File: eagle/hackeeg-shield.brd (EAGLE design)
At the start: 101.6 x 53.3 mm, 145 parts, among them IC1 ADS1299IPAG, IC10 TXB0108PWR, IC11 TXB0108PWR, IC2 TPS72325DBVT, IC3 TPS73225DBVT, IC5 24AA256UID, IC6 TPS60403DBVT, IC7 OPA376DBV, IC8 OPA376DBV, IC9 TXS0102DCUR

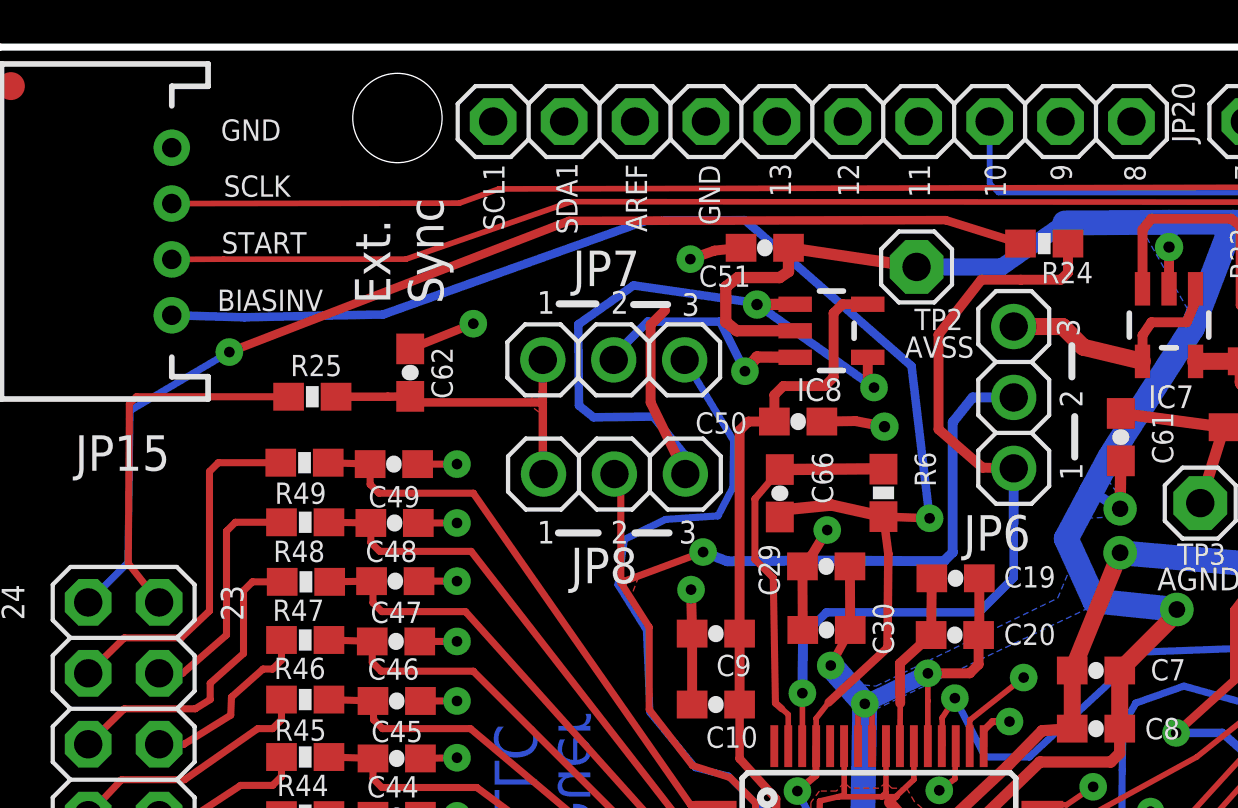
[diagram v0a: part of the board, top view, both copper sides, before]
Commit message: add option to put biasout on ext sync connector
- probably won't use this option, saving it just in case
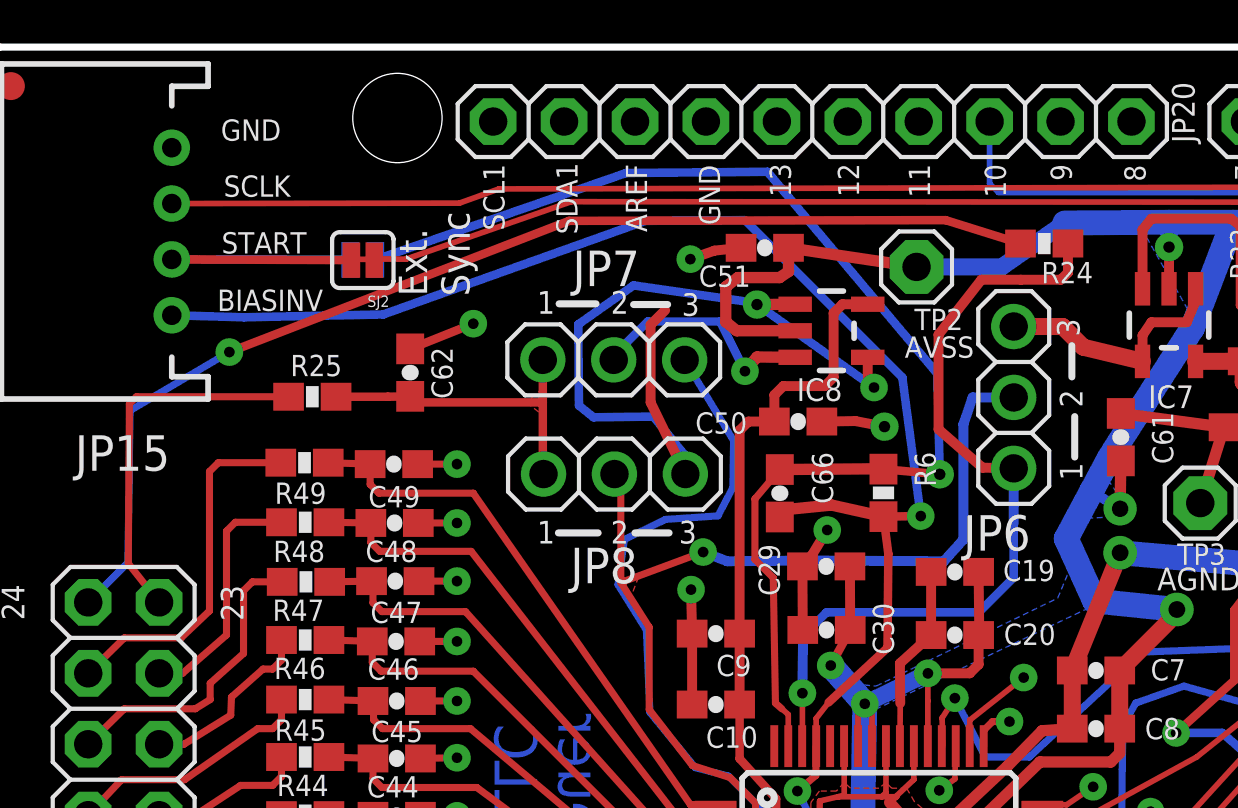
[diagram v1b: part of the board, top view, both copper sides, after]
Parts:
- added SJ1: SOLDERJUMPERNO, SparkFun-Passives:SJ_2S-NO
- added SJ2: SOLDERJUMPERNC, SparkFun-Passives:SJ_2S
- moved C19 0.23 mm to (35.3, 34.7)
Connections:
- new net SYNC_CONN_2: JP15.2, SJ1.2, SJ2.2
- net ADS_START: now also SJ2.1; no longer JP15.2
- net BIASOUT: now also SJ1.1
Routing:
- net BIASOUT: track 14.4 -> 44.1 mm, vias 0 -> 1
- net SYNC_CONN_2: track 0.00 -> 12.8 mm
- net ADS_START: track 118.6 -> 111.4 mm
- net N$22: track 0.00 -> 0.90 mm
- net BIASINV: track 89.9 -> 89.2 mm
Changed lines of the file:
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@@
 <layer number="20" name="Dimension" color="15" fill="1" visible="yes" active="yes"/>
 <layer number="21" name="tPlace" color="7" fill="1" visible="yes" active="yes"/>
-<layer number="22" name="bPlace" color="7" fill="1" visible="no" active="yes"/>
+<layer number="22" name="bPlace" color="7" fill="1" visible="yes" active="yes"/>
 <layer number="23" name="tOrigins" color="15" fill="1" visible="yes" active="yes"/>
-<layer number="24" name="bOrigins" color="15" fill="1" visible="no" active="yes"/>
+<layer number="24" name="bOrigins" color="15" fill="1" visible="yes" active="yes"/>
 <layer number="25" name="tNames" color="7" fill="1" visible="yes" active="yes"/>
 <layer number="26" name="bNames" color="7" fill="1" visible="no" active="yes"/>
@@
 <text x="62.0522" y="23.9776" size="0.8128" layer="21" font="vector" ratio="12" rot="R90">RST</text>
 <text x="9.144" y="48.1076" size="0.762" layer="21" font="vector" ratio="12">SCLK</text>
-<text x="17.018" y="44.2722" size="1.27" layer="21" font="vector" ratio="12" rot="R90">Ext.
+<text x="17.955515625" y="44.54880625" size="1.016" layer="21" font="vector" ratio="12" rot="R90">Ext.
 Sync</text>
 <text x="9.0424" y="50.1142" size="0.762" layer="21" font="vector" ratio="12">GND</text>
@@
 <attribute name="VALUE" x="36.068" y="14.1478" size="0.4064" layer="27" font="vector" rot="R270"/>
 </element>
-<element name="C19" library="SparkFun-Passives" package="0603-CAP" value="1uF" x="35.3568" y="34.4424" smashed="yes">
-<attribute name="NAME" x="37.084" y="34.1122" size="0.762" layer="25" font="vector" ratio="12"/>
-<attribute name="VALUE" x="34.3408" y="33.2994" size="0.4064" layer="27" font="vector"/>
+<element name="C19" library="SparkFun-Passives" package="0603-CAP" value="1uF" x="35.3314" y="34.671" smashed="yes">
+<attribute name="NAME" x="37.0586" y="34.3408" size="0.762" layer="25" font="vector" ratio="12"/>
+<attribute name="VALUE" x="34.3154" y="33.528" size="0.4064" layer="27" font="vector"/>
 </element>
 <element name="C20" library="SparkFun-Passives" package="0603-CAP" value="0.1uF" x="35.3314" y="32.4104" smashed="yes">
@@
 <attribute name="VALUE" x="26.449015625" y="4.865871875" size="1.27" layer="27"/>
 </element>
+<element name="SJ1" library="SparkFun-Passives" package="SJ_2S-NO" value="SOLDERJUMPERNO" x="14.124690625" y="45.848521875" rot="MR0"/>
+<element name="SJ2" library="SparkFun-Passives" package="SJ_2S" value="SOLDERJUMPERNC" x="14.1279875" y="45.8381125" rot="R180"/>
 </elements>
 <signals>
@@
 <contactref element="C19" pad="1"/>
 <contactref element="IC1" pad="55"/>
-<wire x1="34.5068" y1="34.4424" x2="34.4814" y2="32.4104" width="0.3556" layer="1"/>
+<wire x1="34.4814" y1="34.671" x2="34.4814" y2="32.4104" width="0.3556" layer="1"/>
 <wire x1="34.4814" y1="32.4104" x2="33.3636" y2="31.3942" width="0.3556" layer="1"/>
 <wire x1="33.3636" y1="31.3942" x2="33.3756" y2="29.972" width="0.3556" layer="1"/>
@@
 <wire x1="23.368" y1="37.7952" x2="23.1394" y2="38.1762" width="0.254" layer="1"/>
 <wire x1="30.1498" y1="35.0774" x2="34.936121875" y2="35.0535875" width="0.3556" layer="16"/>
-<wire x1="34.936121875" y1="35.0535875" x2="35.2552" y2="35.371084375" width="0.3556" layer="16"/>
-<wire x1="35.2552" y1="35.371084375" x2="35.2552" y2="40.0304" width="0.3556" layer="16"/>
-<wire x1="35.2552" y1="40.0304" x2="35.9664" y2="40.9194" width="0.3556" layer="16"/>
+<wire x1="34.936121875" y1="35.0535875" x2="35.6362" y2="35.828284375" width="0.3556" layer="16"/>
+<wire x1="35.6362" y1="35.828284375" x2="35.6362" y2="39.9542" width="0.3556" layer="16"/>
+<wire x1="35.6362" y1="39.9542" x2="35.9664" y2="40.9194" width="0.3556" layer="16"/>
 <wire x1="27.178" y1="35.052" x2="30.1498" y2="35.0774" width="0.3556" layer="16"/>
 <wire x1="26.3144" y1="35.3822" x2="27.178" y2="35.052" width="0.3556" layer="16"/>
@@
 <wire x1="86.741" y1="25.4" x2="86.741" y2="22.86" width="0.254" layer="16"/>
 <wire x1="54.8856" y1="23.5712" x2="54.8608" y2="23.596" width="0.2032" layer="1"/>
-<wire x1="9.143" y1="45.8724" x2="15.6718" y2="45.8724" width="0.2032" layer="1"/>
+<wire x1="14.796021875" y1="45.8764625" x2="15.6718" y2="45.8724" width="0.2032" layer="1"/>
 <wire x1="15.6718" y1="45.8724" x2="21.59" y2="47.9298" width="0.2032" layer="1"/>
 <wire x1="21.59" y1="47.9298" x2="62.8523" y2="47.9044" width="0.2032" layer="1"/>
@@
 <wire x1="83.185" y1="24.1046" x2="82.3976" y2="24.892" width="0.2032" layer="1"/>
 <wire x1="82.3976" y1="24.892" x2="82.3976" y2="25.527" width="0.2032" layer="1"/>
-<contactref element="JP15" pad="2"/>
-<wire x1="7.286" y1="45.863" x2="9.143" y2="45.8724" width="0.2032" layer="1"/>
+<contactref element="SJ2" pad="1"/>
+<wire x1="14.796021875" y1="45.8764625" x2="14.5398875" y2="45.8381125" width="0.2032" layer="1"/>
 </signal>
 <signal name="N$14">
@@
 <wire x1="36.1814" y1="31.3563" x2="35.8639" y2="31.0388" width="0.3556" layer="1"/>
 <wire x1="35.8639" y1="31.0388" x2="34.3662" y2="31.0388" width="0.3556" layer="1"/>
-<wire x1="36.2068" y1="34.4424" x2="36.2068" y2="32.4358" width="0.3556" layer="1"/>
+<wire x1="36.1814" y1="34.671" x2="36.2068" y2="32.4358" width="0.3556" layer="1"/>
 <wire x1="36.2068" y1="32.4358" x2="36.1814" y2="32.4104" width="0.3556" layer="1"/>
 <via x="43.2816" y="33.3248" extent="1-16" drill="0.6"/>
@@
 <contactref element="JP15" pad="1"/>
 <wire x1="24.257" y1="47.244" x2="27.813" y2="47.2694" width="0.3048" layer="16"/>
-<wire x1="27.813" y1="47.2694" x2="33.780475" y2="42.04335" width="0.3048" layer="16"/>
-<via x="34.42715625" y="36.591746875" extent="1-16" drill="0.381"/>
-<wire x1="34.42715625" y1="36.591746875" x2="33.780475" y2="42.04335" width="0.3048" layer="16"/>
+<wire x1="27.813" y1="47.2694" x2="33.450275" y2="41.63695" width="0.3048" layer="16"/>
+<via x="34.1101625" y="36.67099375" extent="1-16" drill="0.381"/>
+<wire x1="34.1101625" y1="36.67099375" x2="33.450275" y2="41.63695" width="0.3048" layer="16"/>
 <contactref element="JP16" pad="3"/>
 <wire x1="14.859" y1="43.8912" x2="9.8806" y2="43.7896" width="0.3048" layer="16"/>
@@
 <wire x1="30.912309375" y1="37.065459375" x2="32.774890625" y2="36.650809375" width="0.4064" layer="1"/>
 <wire x1="32.948628125" y1="35.3164125" x2="32.774890625" y2="36.650809375" width="0.3048" layer="1"/>
-<wire x1="32.774890625" y1="36.650809375" x2="34.42715625" y2="36.591746875" width="0.3048" layer="1"/>
+<wire x1="32.774890625" y1="36.650809375" x2="34.1101625" y2="36.67099375" width="0.3048" layer="1"/>
 </signal>
 <signal name="BIASOUT">
@@
 <wire x1="29.062425" y1="38.33760625" x2="32.495490625" y2="38.36300625" width="0.4064" layer="1"/>
 <wire x1="32.495490625" y1="38.36300625" x2="32.774890625" y2="38.350809375" width="0.4064" layer="1"/>
+<contactref element="SJ1" pad="1"/>
+<wire x1="14.574690625" y1="45.848521875" x2="23.55723125" y2="48.95723125" width="0.3048" layer="16"/>
+<wire x1="23.55723125" y1="48.95723125" x2="28.617671875" y2="49.001171875" width="0.3048" layer="16"/>
+<wire x1="28.617671875" y1="49.001171875" x2="34.7050375" y2="41.768521875" width="0.3048" layer="16"/>
+<wire x1="34.7050375" y1="41.768521875" x2="34.79139375" y2="38.167309375" width="0.3048" layer="16"/>
+<via x="34.79139375" y="38.167309375" extent="1-16" drill="0.4064" diameter="0.254"/>
+<wire x1="34.79139375" y1="38.167309375" x2="32.774890625" y2="38.350809375" width="0.3048" layer="1"/>
 </signal>
 <signal name="VCC_5V_FILTERED">
@@
 </polygon>
 </signal>
+<signal name="SYNC_CONN_2">
+<contactref element="JP15" pad="2"/>
+<contactref element="SJ1" pad="2"/>
+<contactref element="SJ2" pad="2"/>
+<wire x1="7.286" y1="45.863" x2="13.674690625" y2="45.848521875" width="0.3048" layer="16"/>
+<wire x1="13.7160875" y1="45.8381125" x2="7.286" y2="45.863" width="0.3048" layer="1"/>
+</signal>
+<signal name="N$22">
+<wire x1="13.71955625" y1="45.8668125" x2="14.615921875" y2="45.8668125" width="0.2032" layer="1"/>
+</signal>
 </signals>
